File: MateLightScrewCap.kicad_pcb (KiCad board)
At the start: 2 copper layers, 24 x 24 mm, 5 parts, among them X1 IN, X2 OUT, X3 Power, X4 Power

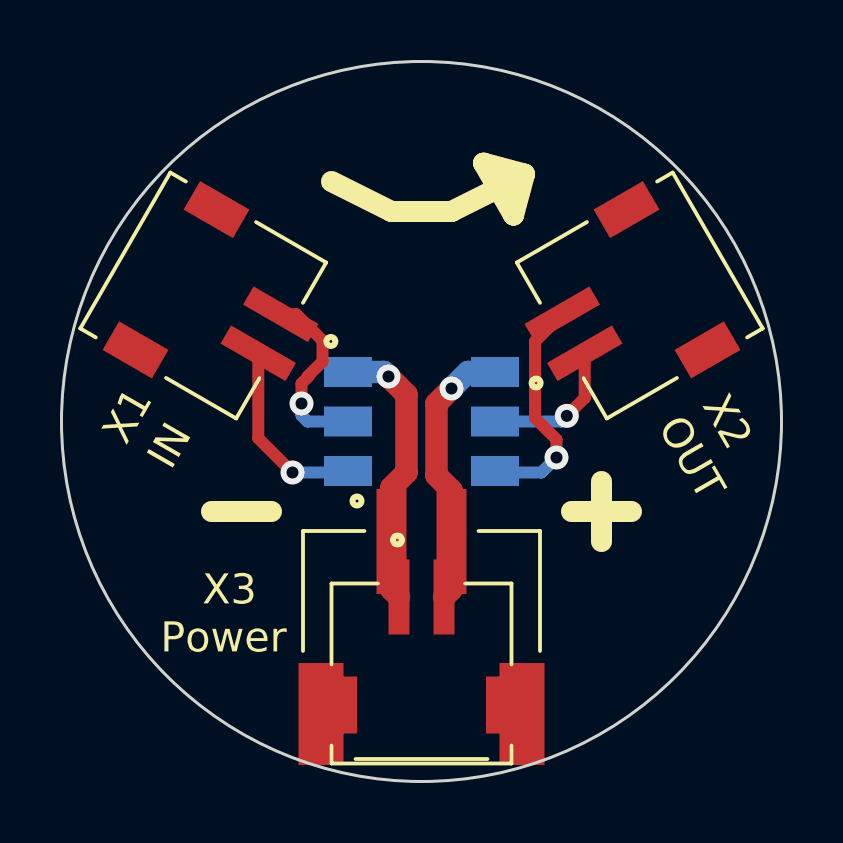
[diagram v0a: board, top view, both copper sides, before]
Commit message: Port project to KiCad v6 + Small changes
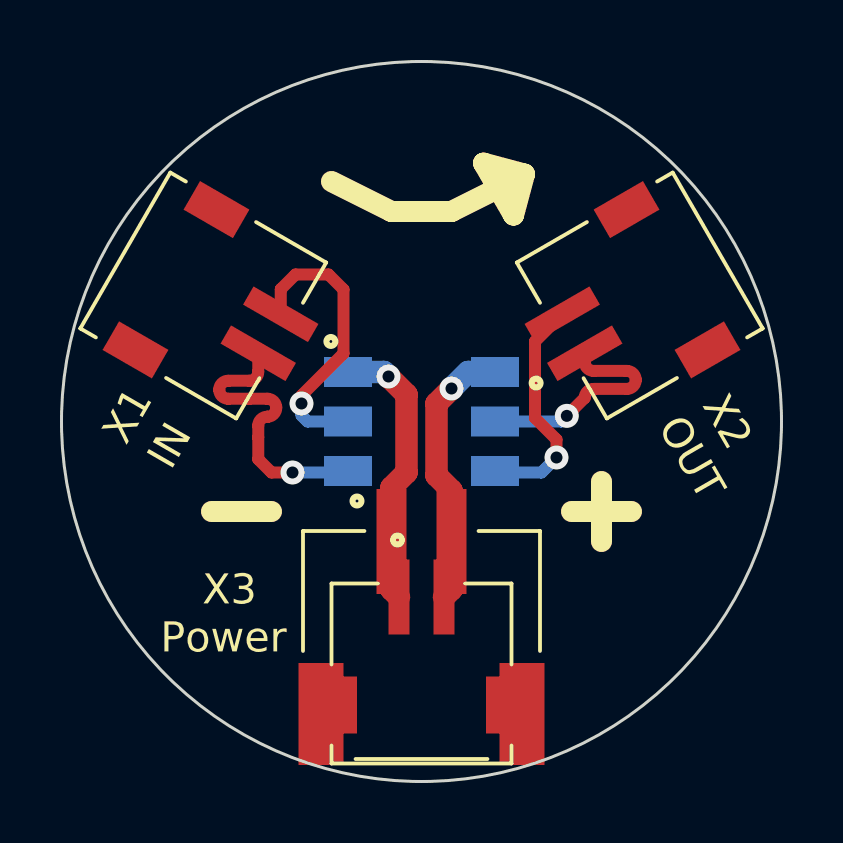
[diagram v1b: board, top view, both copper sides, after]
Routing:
- net /CKI: track 6.29 -> 9.75 mm
- net /SDI: track 6.32 -> 9.68 mm
- net /CKO: track 4.81 -> 7.64 mm
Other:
- net class Default removed
- net class Power removed

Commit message: Optimized data tracks to exact same length
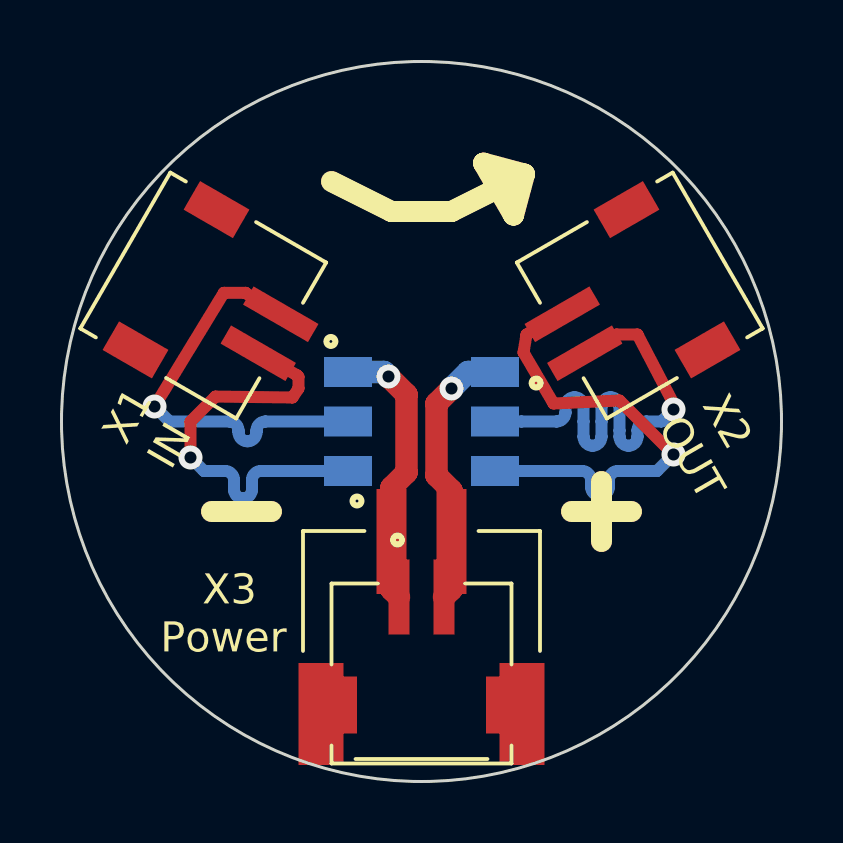
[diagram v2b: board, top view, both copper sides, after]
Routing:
- net /SDO: track 7.72 -> 16.0 mm
- net /CKO: track 7.64 -> 15.9 mm
- net /SDI: track 9.68 -> 14.0 mm
- net /CKI: track 9.75 -> 14.0 mm
